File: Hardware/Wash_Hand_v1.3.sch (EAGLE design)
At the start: 30 parts, among them J1 I2C, J2 ICSP, J3 SPI, J5 EXT_VCC, Q1 16.0 Mhz, U1 328P

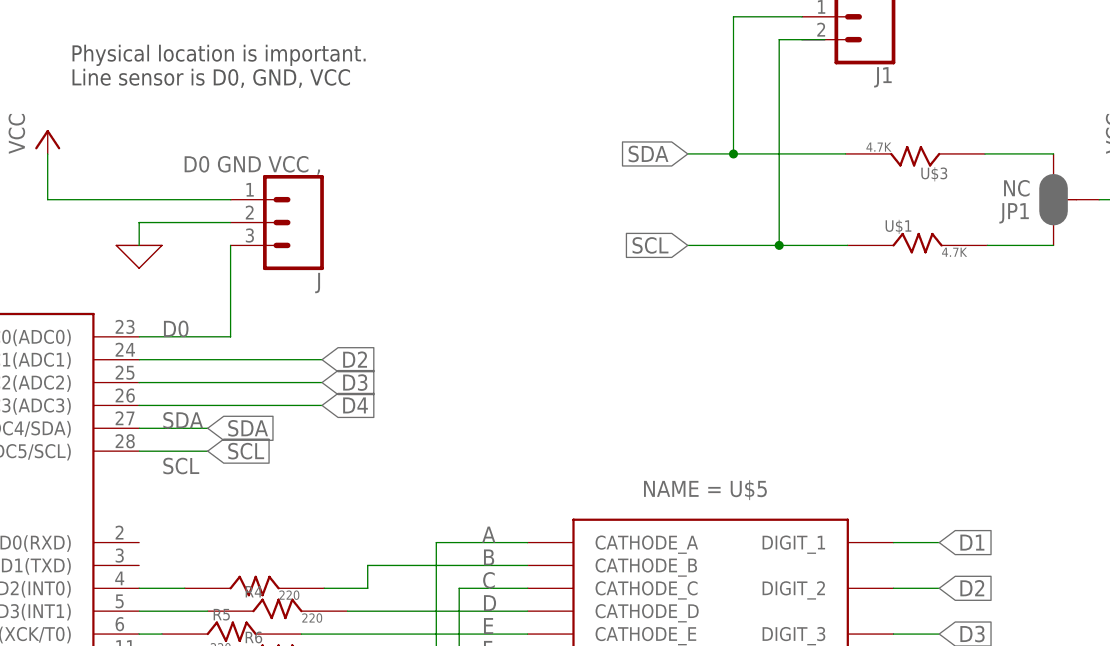
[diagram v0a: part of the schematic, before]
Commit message: Schematic/Board: Add registers name on SCL/SCK
Signed-off-by: Konrad Rzeszutek Wilk <konrad@kernel.org>
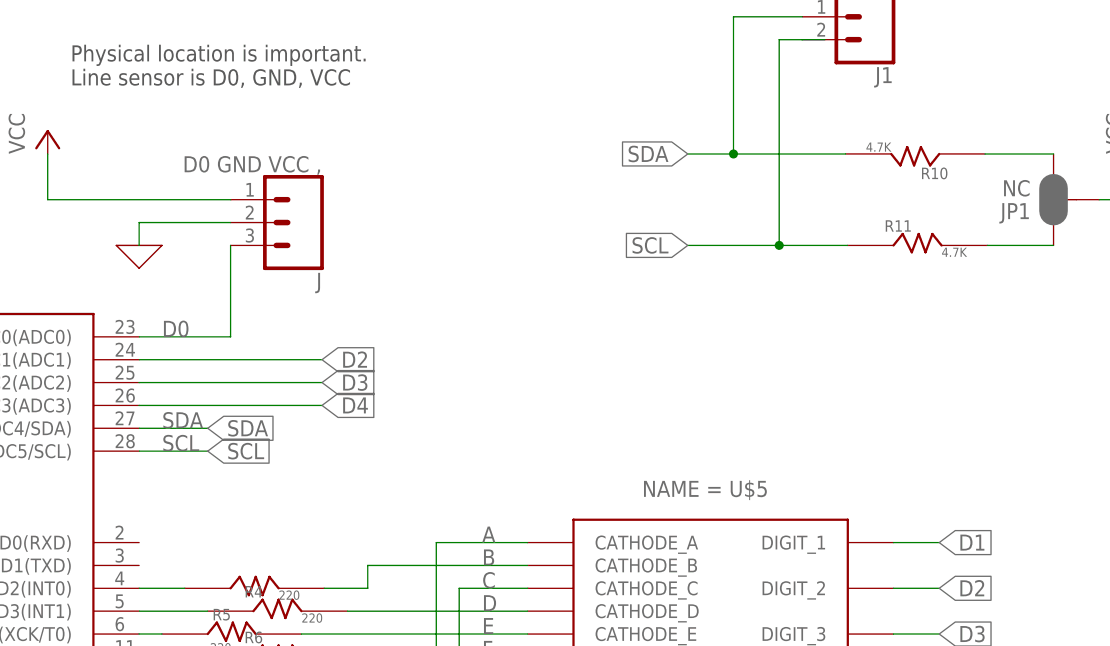
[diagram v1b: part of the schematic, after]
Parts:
- renumbered U$1 to R11, U$3 to R10
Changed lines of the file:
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@@
 <part name="J5" library="SparkFun-Connectors" library_urn="urn:adsk.eagle:library:513" deviceset="CONN_02" device="" package3d_urn="urn:adsk.eagle:package:38039/1" value="EXT_VCC"/>
 <part name="H6" library="SparkFun-Hardware" library_urn="urn:adsk.eagle:library:519" deviceset="STAND-OFF" device="" package3d_urn="urn:adsk.eagle:package:38630/1"/>
-<part name="U$3" library="darnok_common" deviceset="RESISTOR" device="R1206" value="4.7K"/>
-<part name="U$1" library="darnok_common" deviceset="RESISTOR" device="R1206" value="4.7K"/>
+<part name="R10" library="darnok_common" deviceset="RESISTOR" device="R1206" value="4.7K"/>
+<part name="R11" library="darnok_common" deviceset="RESISTOR" device="R1206" value="4.7K"/>
 <part name="JP1" library="SparkFun-Jumpers" library_urn="urn:adsk.eagle:library:528" deviceset="JUMPER-SMT_3_2-NC_PASTE" device="_SILK" package3d_urn="urn:adsk.eagle:package:39294/1" value="NC"/>
 <part name="P+6" library="supply1" library_urn="urn:adsk.eagle:library:371" deviceset="VCC" device=""/>
@@
 </instance>
 <instance part="H6" gate="G$1" x="170.18" y="60.96" smashed="yes"/>
-<instance part="U$3" gate="G$1" x="205.74" y="177.8" smashed="yes" rot="R180">
+<instance part="R10" gate="G$1" x="205.74" y="177.8" smashed="yes" rot="R180">
 <attribute name="NAME" x="206.756" y="176.276" size="1.27" layer="95" rot="R180"/>
 <attribute name="VALUE" x="200.406" y="179.07" size="1.016" layer="96" rot="R180"/>
 </instance>
-<instance part="U$1" gate="G$1" x="200.66" y="167.64" smashed="yes">
+<instance part="R11" gate="G$1" x="200.66" y="167.64" smashed="yes">
 <attribute name="NAME" x="199.644" y="169.164" size="1.27" layer="95"/>
 <attribute name="VALUE" x="205.994" y="166.37" size="1.016" layer="96"/>
@@
 </segment>
 <segment>
-<pinref part="U$3" gate="G$1" pin="R_2"/>
+<pinref part="R10" gate="G$1" pin="R_2"/>
 <pinref part="J1" gate="G$1" pin="1"/>
 <wire x1="182.88" y1="193.04" x2="190.5" y2="193.04" width="0.1524" layer="91"/>
@@
 <pinref part="U1" gate="G$1" pin="PC5(ADC5/SCL)"/>
 <wire x1="124.46" y1="144.78" x2="116.84" y2="144.78" width="0.1524" layer="91"/>
-<label x="119.38" y="142.24" size="1.778" layer="95"/>
+<label x="119.38" y="144.78" size="1.778" layer="95"/>
 <label x="124.46" y="144.78" size="1.778" layer="95" xref="yes"/>
 </segment>
 <segment>
-<pinref part="U$1" gate="G$1" pin="R_1"/>
+<pinref part="R11" gate="G$1" pin="R_1"/>
 <pinref part="J1" gate="G$1" pin="2"/>
 <wire x1="190.5" y1="190.5" x2="193.04" y2="190.5" width="0.1524" layer="91"/>
@@
 <net name="N$5" class="0">
 <segment>
-<pinref part="U$3" gate="G$1" pin="R_1"/>
+<pinref part="R10" gate="G$1" pin="R_1"/>
 <pinref part="JP1" gate="G$1" pin="3"/>
 <wire x1="210.82" y1="177.8" x2="218.44" y2="177.8" width="0.1524" layer="91"/>
@@
 <net name="N$6" class="0">
 <segment>
-<pinref part="U$1" gate="G$1" pin="R_2"/>
+<pinref part="R11" gate="G$1" pin="R_2"/>
 <pinref part="JP1" gate="G$1" pin="1"/>
 <wire x1="211.074" y1="167.64" x2="218.44" y2="167.64" width="0.1524" layer="91"/>

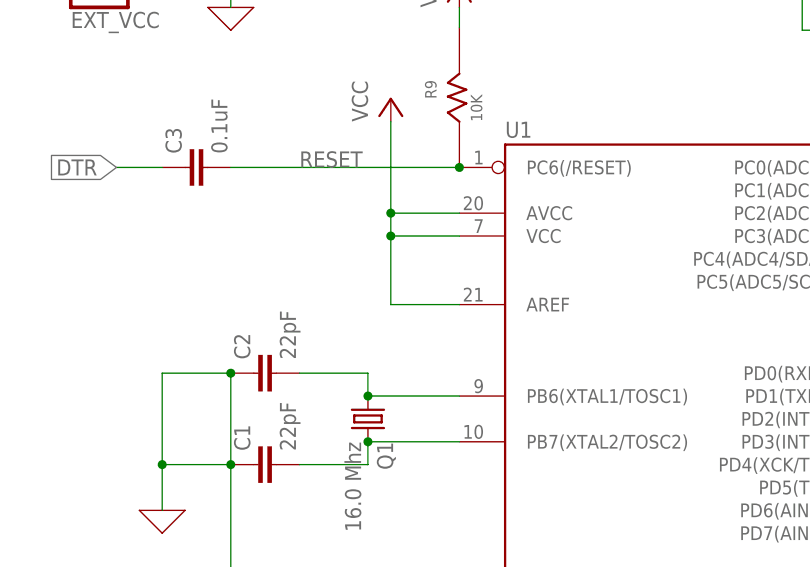
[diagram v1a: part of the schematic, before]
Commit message: Schematic: Add decoupling capacitor on the VREF.
Signed-off-by: Konrad Rzeszutek Wilk <konrad@kernel.org>
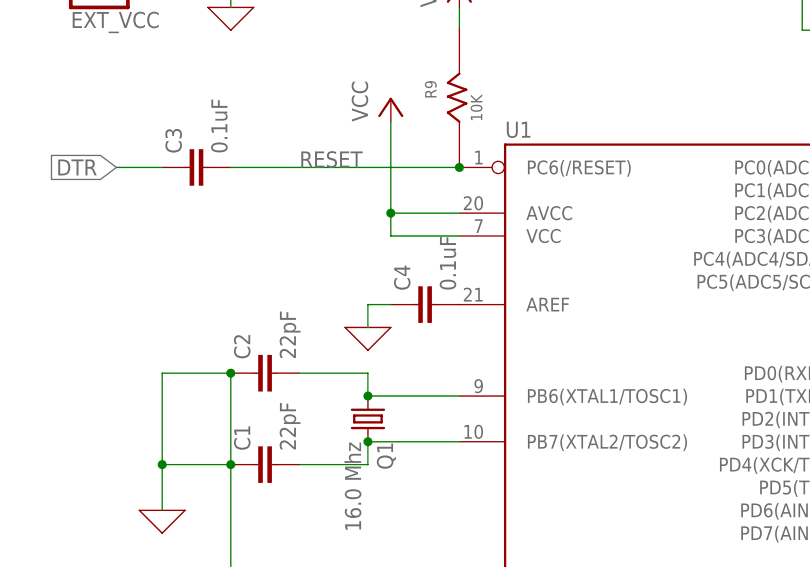
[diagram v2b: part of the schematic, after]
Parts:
- added C4: 0.1uF, SparkFun-Capacitors:1.0UF-1206-50V-10%
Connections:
- net 0: now also C4.1
- net VCC: no longer U1.AREF
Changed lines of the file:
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@@
 <part name="P+7" library="supply1" library_urn="urn:adsk.eagle:library:371" deviceset="VCC" device=""/>
 <part name="C3" library="SparkFun-Capacitors" library_urn="urn:adsk.eagle:library:510" deviceset="1.0UF" device="-1206-50V-10%" package3d_urn="urn:adsk.eagle:package:37426/1" value="0.1uF"/>
+<part name="C4" library="SparkFun-Capacitors" library_urn="urn:adsk.eagle:library:510" deviceset="1.0UF" device="-1206-50V-10%" package3d_urn="urn:adsk.eagle:package:37426/1" value="0.1uF"/>
+<part name="X_7" library="ngspice-simulation" library_urn="urn:adsk.eagle:library:527439" deviceset="GND" device=""/>
 </parts>
 <sheets>
@@
 <attribute name="VALUE" x="42.799" y="159.004" size="1.778" layer="96" font="vector" rot="R90"/>
 </instance>
+<instance part="C4" gate="G$1" x="66.04" y="142.24" smashed="yes" rot="R90">
+<attribute name="NAME" x="63.119" y="143.764" size="1.778" layer="95" font="vector" rot="R90"/>
+<attribute name="VALUE" x="68.199" y="143.764" size="1.778" layer="96" font="vector" rot="R90"/>
+</instance>
+<instance part="X_7" gate="G$1" x="58.42" y="139.7" smashed="yes"/>
 </instances>
 <busses>
@@
 <pinref part="U1" gate="G$1" pin="AVCC"/>
 <wire x1="68.58" y1="152.4" x2="60.96" y2="152.4" width="0.1524" layer="91"/>
-<pinref part="U1" gate="G$1" pin="AREF"/>
-<wire x1="68.58" y1="142.24" x2="60.96" y2="142.24" width="0.1524" layer="91"/>
-<wire x1="60.96" y1="142.24" x2="60.96" y2="149.86" width="0.1524" layer="91"/>
 <wire x1="60.96" y1="149.86" x2="60.96" y2="152.4" width="0.1524" layer="91"/>
 <pinref part="U1" gate="G$1" pin="VCC"/>
 <wire x1="68.58" y1="149.86" x2="60.96" y2="149.86" width="0.1524" layer="91"/>
-<junction x="60.96" y="149.86"/>
 <pinref part="P+1" gate="VCC" pin="VCC"/>
 <wire x1="60.96" y1="152.4" x2="60.96" y2="162.56" width="0.1524" layer="91"/>
@@
 <wire x1="43.18" y1="177.8" x2="43.18" y2="175.26" width="0.1524" layer="91"/>
 </segment>
+<segment>
+<pinref part="C4" gate="G$1" pin="1"/>
+<wire x1="60.96" y1="142.24" x2="58.42" y2="142.24" width="0.1524" layer="91"/>
+<pinref part="X_7" gate="G$1" pin="0"/>
+<wire x1="58.42" y1="139.7" x2="58.42" y2="142.24" width="0.1524" layer="91"/>
+</segment>
 </net>

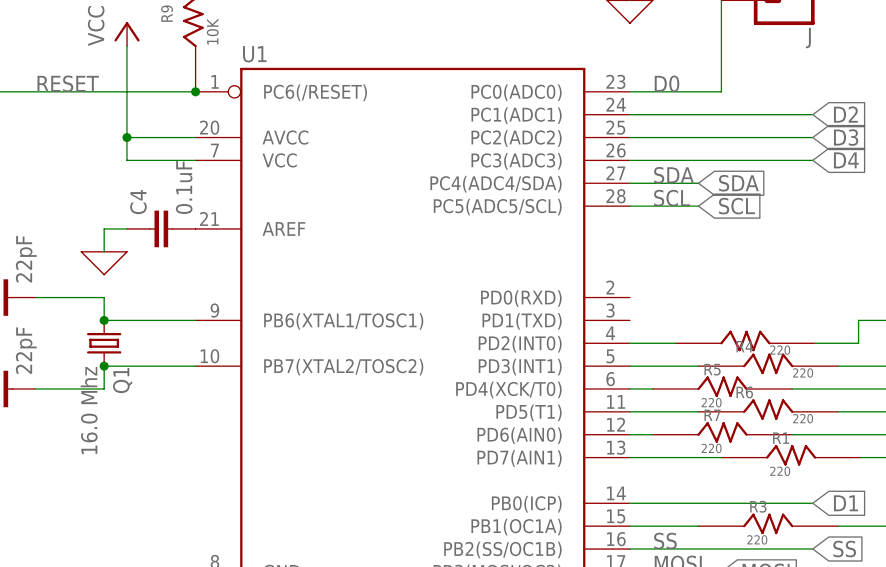
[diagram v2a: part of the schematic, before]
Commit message: Schematic: Add the TX/RX labels
Signed-off-by: Konrad Rzeszutek Wilk <konrad@kernel.org>
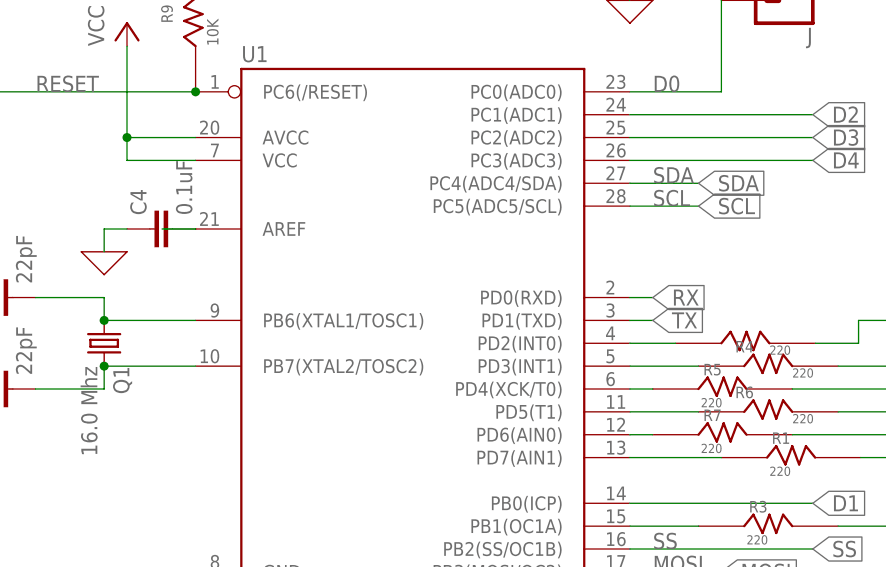
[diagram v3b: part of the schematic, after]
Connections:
- new net N$2: C4.2, U1.AREF
- new net RX: U1.PD0(RXD)
- new net TX: U1.PD1(TXD)
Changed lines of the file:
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@@
+</segment>
+</net>
+<net name="TX" class="0">
+<segment>
+<pinref part="U1" gate="G$1" pin="PD1(TXD)"/>
+<wire x1="116.84" y1="132.08" x2="119.38" y2="132.08" width="0.1524" layer="91"/>
+<label x="119.38" y="132.08" size="1.778" layer="95" xref="yes"/>
+</segment>
+</net>
+<net name="RX" class="0">
+<segment>
+<pinref part="U1" gate="G$1" pin="PD0(RXD)"/>
+<wire x1="116.84" y1="134.62" x2="119.38" y2="134.62" width="0.1524" layer="91"/>
+<label x="119.38" y="134.62" size="1.778" layer="95" xref="yes"/>
+</segment>
+</net>
+<net name="N$2" class="0">
+<segment>
+<pinref part="U1" gate="G$1" pin="AREF"/>
+<wire x1="68.58" y1="142.24" x2="64.8462" y2="142.24" width="0.1524" layer="91"/>
+<pinref part="C4" gate="G$1" pin="2"/>
 </segment>
 </net>

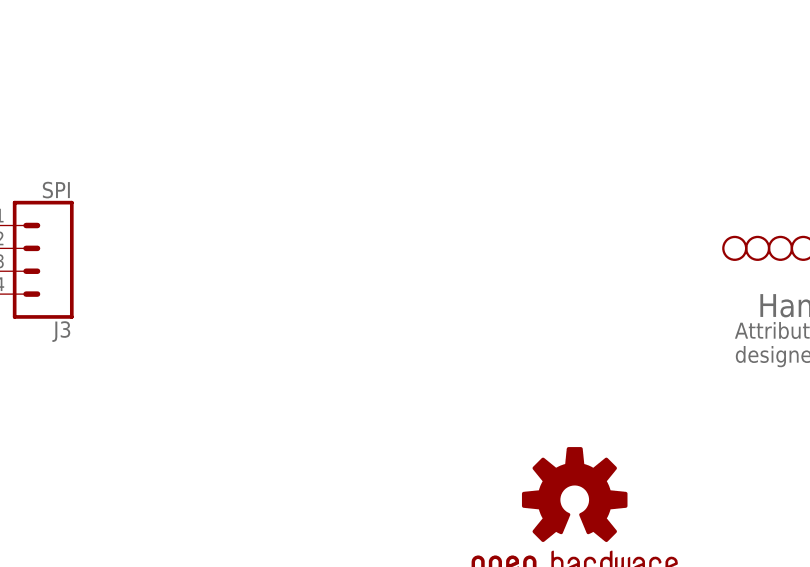
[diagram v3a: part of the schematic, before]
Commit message: Board: Add FTDI basic (6 pin).
And connect them all.

Signed-off-by: Konrad Rzeszutek Wilk <konrad@kernel.org>
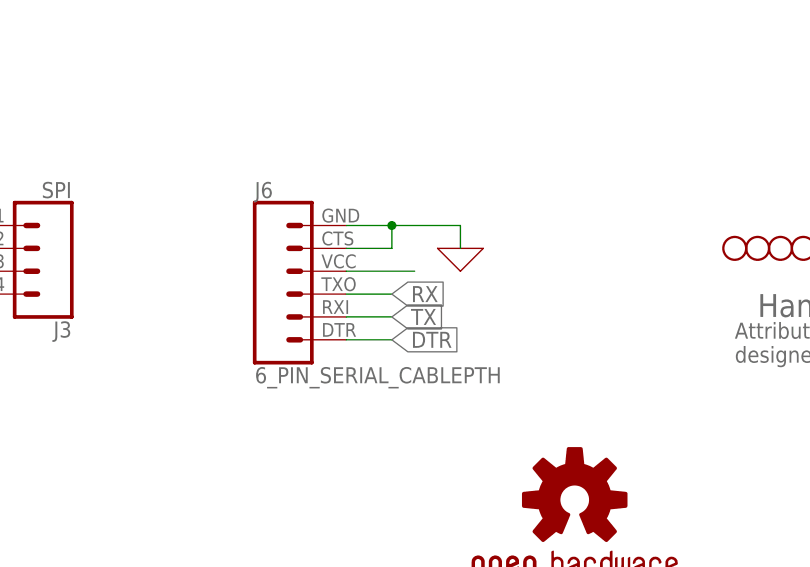
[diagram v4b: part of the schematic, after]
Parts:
- added J6: 6_PIN_SERIAL_CABLEPTH, SparkFun-Connectors:6_PIN_SERIAL_CABLEPTH
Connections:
- new net N$13: J6.4
- net 0: now also J6.5, J6.6
- net DTR: now also J6.1
- net RX: now also J6.3
- net TX: now also J6.2
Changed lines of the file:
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@@
 <part name="C4" library="SparkFun-Capacitors" library_urn="urn:adsk.eagle:library:510" deviceset="1.0UF" device="-1206-50V-10%" package3d_urn="urn:adsk.eagle:package:37426/1" value="0.1uF"/>
 <part name="X_7" library="ngspice-simulation" library_urn="urn:adsk.eagle:library:527439" deviceset="GND" device=""/>
+<part name="J6" library="SparkFun-Connectors" library_urn="urn:adsk.eagle:library:513" deviceset="6_PIN_SERIAL_CABLE" device="PTH" package3d_urn="urn:adsk.eagle:package:38027/1"/>
+<part name="X_8" library="ngspice-simulation" library_urn="urn:adsk.eagle:library:527439" deviceset="GND" device=""/>
 </parts>
 <sheets>
@@
 </instance>
 <instance part="X_7" gate="G$1" x="58.42" y="139.7" smashed="yes"/>
+<instance part="J6" gate="G$1" x="109.22" y="55.88" smashed="yes">
+<attribute name="VALUE" x="104.14" y="45.974" size="1.778" layer="96" font="vector"/>
+<attribute name="NAME" x="104.14" y="66.548" size="1.778" layer="95" font="vector"/>
+</instance>
+<instance part="X_8" gate="G$1" x="127" y="60.96" smashed="yes"/>
 </instances>
 <busses>
@@
 <wire x1="58.42" y1="139.7" x2="58.42" y2="142.24" width="0.1524" layer="91"/>
 </segment>
+<segment>
+<pinref part="J6" gate="G$1" pin="5"/>
+<wire x1="114.3" y1="60.96" x2="119.38" y2="60.96" width="0.1524" layer="91"/>
+<pinref part="J6" gate="G$1" pin="6"/>
+<wire x1="114.3" y1="63.5" x2="119.38" y2="63.5" width="0.1524" layer="91"/>
+<wire x1="119.38" y1="60.96" x2="119.38" y2="63.5" width="0.1524" layer="91"/>
+<wire x1="119.38" y1="63.5" x2="127" y2="63.5" width="0.1524" layer="91"/>
+<junction x="119.38" y="63.5"/>
+<wire x1="127" y1="63.5" x2="127" y2="60.96" width="0.1524" layer="91"/>
+<pinref part="X_8" gate="G$1" pin="0"/>
+</segment>
 </net>
 <net name="N$8" class="0">
@@
 <label x="20.32" y="58.42" size="1.778" layer="95" rot="R180" xref="yes"/>
 </segment>
+<segment>
+<pinref part="J6" gate="G$1" pin="1"/>
+<wire x1="114.3" y1="50.8" x2="119.38" y2="50.8" width="0.1524" layer="91"/>
+<label x="119.38" y="50.8" size="1.778" layer="95" xref="yes"/>
+</segment>
 </net>
 <net name="TX" class="0">
@@
 <label x="119.38" y="132.08" size="1.778" layer="95" xref="yes"/>
 </segment>
+<segment>
+<pinref part="J6" gate="G$1" pin="2"/>
+<wire x1="114.3" y1="53.34" x2="119.38" y2="53.34" width="0.1524" layer="91"/>
+<label x="119.38" y="53.34" size="1.778" layer="95" xref="yes"/>
+</segment>
 </net>
 <net name="RX" class="0">
@@
 <label x="119.38" y="134.62" size="1.778" layer="95" xref="yes"/>
 </segment>
+<segment>
+<pinref part="J6" gate="G$1" pin="3"/>
+<wire x1="114.3" y1="55.88" x2="119.38" y2="55.88" width="0.1524" layer="91"/>
+<label x="119.38" y="55.88" size="1.778" layer="95" xref="yes"/>
+</segment>
 </net>
 <net name="N$2" class="0">
@@
 </segment>
 </net>
+<net name="N$13" class="0">
+<segment>
+<pinref part="J6" gate="G$1" pin="4"/>
+<wire x1="114.3" y1="58.42" x2="121.92" y2="58.42" width="0.1524" layer="91"/>
+</segment>
+</net>
